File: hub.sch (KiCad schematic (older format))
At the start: 22 parts, among them J1 USB_C_Receptacle_USB2.0, J6 Conn_01x03, U14 GL850G, U15 K24C02D-O, X2 ECS-2520MV-120-xx

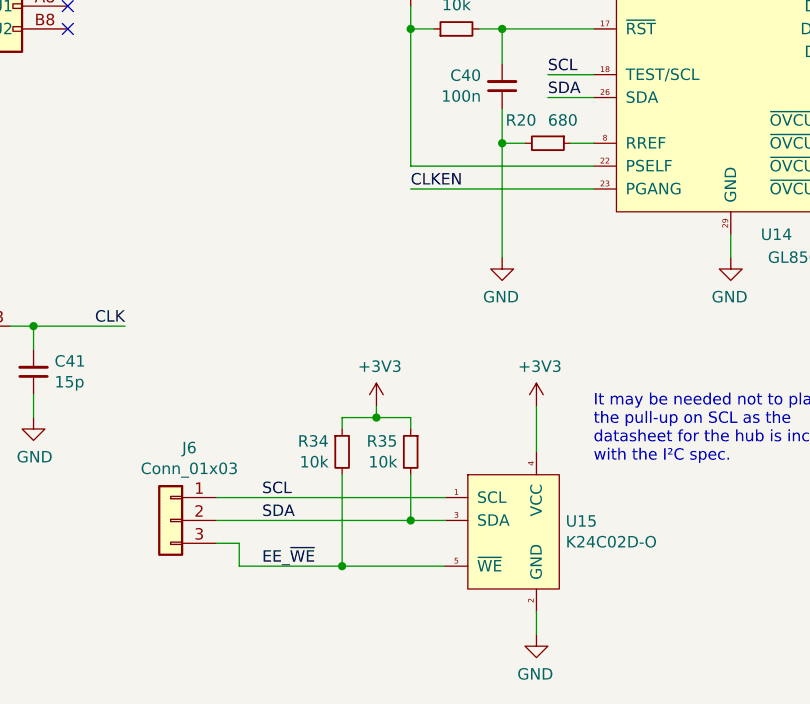
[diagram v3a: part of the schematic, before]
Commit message: sch, pcb: Fix hub startup and use smaller crystals
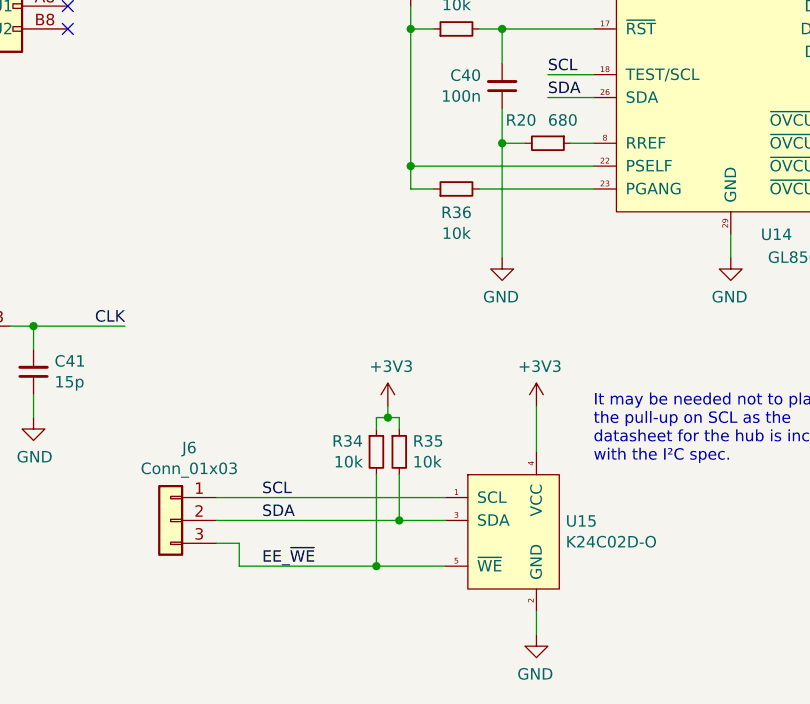
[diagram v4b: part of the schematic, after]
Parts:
- added R36: 10k, Resistor_SMD:R_0603_1608Metric, symbol Device:R_Small
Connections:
- net +3V3: now also R36.1
- net CLKEN: no longer names the net of U14.23 (PGANG)
- net CLKEN: now also R36.2
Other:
- moved on the sheet: R34, R35
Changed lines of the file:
@@
 Wire Wire Line
 	6350 3600 5950 3600
-Wire Wire Line
-	6350 4600 5550 4600
-Text Label 5550 4600 0    50   ~ 0
-CLKEN
 Text Label 5950 3600 0    50   ~ 0
 CLK
@@
 SDA
 $Comp
-L Device:R_Small R?
-U 1 1 5E1E7739
-P 5550 5750
-AR Path="/5DF7E971/5E1E7739" Ref="R?"  Part="1"
-AR Path="/5DFC2583/5E1E7739" Ref="R?"  Part="1"
-AR Path="/5E157F68/5E1E7739" Ref="R35"  Part="1"
-F 0 "R35" H 5608 5796 50  0000 L CNN
-F 1 "10k" H 5608 5705 50  0000 L CNN
-F 2 "Resistor_SMD:R_0603_1608Metric" H 5550 5750 50  0001 C CNN
-F 3 "~" H 5550 5750 50  0001 C CNN
-	1    5550 5750
-	-1   0    0    -1
-$EndComp
-Wire Wire Line
-	5550 5650 5550 5600
+L power:+3V3 #PWR058
+U 1 1 5E1E2F22
+P 5450 5550
+F 0 "#PWR058" H 5450 5400 50  0001 C CNN
+F 1 "+3V3" H 5465 5723 50  0000 C CNN
+F 2 "" H 5450 5550 50  0001 C CNN
+F 3 "" H 5450 5550 50  0001 C CNN
+	1    5450 5550
+	1    0    0    -1
+$EndComp
+Wire Wire Line
+	5500 5650 5500 5600
+Wire Wire Line
+	5450 5550 5450 5600
 $Comp
 L Device:R_Small R?
 U 1 1 5E1FC098
-P 5250 5750
+P 5400 5750
 AR Path="/5DF7E971/5E1FC098" Ref="R?"  Part="1"
 AR Path="/5DFC2583/5E1FC098" Ref="R?"  Part="1"
 AR Path="/5E157F68/5E1FC098" Ref="R34"  Part="1"
-F 0 "R34" H 5191 5796 50  0000 R CNN
-F 1 "10k" H 5191 5705 50  0000 R CNN
-F 2 "Resistor_SMD:R_0603_1608Metric" H 5250 5750 50  0001 C CNN
-F 3 "~" H 5250 5750 50  0001 C CNN
-	1    5250 5750
-	1    0    0    -1
-$EndComp
-Wire Wire Line
-	5250 5650 5250 5600
-Wire Wire Line
-	5700 6250 5250 6250
-Wire Wire Line
-	5250 5850 5250 6250
-Connection ~ 5250 6250
-Wire Wire Line
-	5550 5850 5550 6050
-Connection ~ 5550 6050
-Wire Wire Line
-	5550 6050 5700 6050
+F 0 "R34" H 5341 5796 50  0000 R CNN
+F 1 "10k" H 5341 5705 50  0000 R CNN
+F 2 "Resistor_SMD:R_0603_1608Metric" H 5400 5750 50  0001 C CNN
+F 3 "~" H 5400 5750 50  0001 C CNN
+	1    5400 5750
+	1    0    0    -1
+$EndComp
+Wire Wire Line
+	5400 5650 5400 5600
+Wire Wire Line
+	5700 6250 5400 6250
+Wire Wire Line
+	5400 5850 5400 6250
+Connection ~ 5400 6250
+Wire Wire Line
+	5500 5850 5500 6050
+Connection ~ 5500 6050
+Wire Wire Line
+	5500 6050 5700 6050
+Wire Wire Line
+	5400 5600 5450 5600
 Text Label 4900 6250 0    50   ~ 0
 EE_~WE
@@
 	4800 6150 4700 6150
 Wire Wire Line
-	4800 6250 5250 6250
-Wire Wire Line
-	4700 6050 5550 6050
+	4800 6250 5400 6250
+Wire Wire Line
+	4700 6050 5500 6050
+$Comp
+L Device:R_Small R?
+U 1 1 5E1E7739
+P 5500 5750
+AR Path="/5DF7E971/5E1E7739" Ref="R?"  Part="1"
+AR Path="/5DFC2583/5E1E7739" Ref="R?"  Part="1"
+AR Path="/5E157F68/5E1E7739" Ref="R35"  Part="1"
+F 0 "R35" H 5559 5796 50  0000 L CNN
+F 1 "10k" H 5559 5705 50  0000 L CNN
+F 2 "Resistor_SMD:R_0603_1608Metric" H 5500 5750 50  0001 C CNN
+F 3 "~" H 5500 5750 50  0001 C CNN
+	1    5500 5750
+	1    0    0    -1
+$EndComp
 Wire Wire Line
 	4700 5950 5700 5950
-Connection ~ 5400 5600
-Wire Wire Line
-	5250 5600 5400 5600
-Wire Wire Line
-	5400 5600 5550 5600
-Wire Wire Line
-	5400 5550 5400 5600
-$Comp
-L power:+3V3 #PWR058
-U 1 1 5E1E2F22
-P 5400 5550
-F 0 "#PWR058" H 5400 5400 50  0001 C CNN
-F 1 "+3V3" H 5415 5723 50  0000 C CNN
-F 2 "" H 5400 5550 50  0001 C CNN
-F 3 "" H 5400 5550 50  0001 C CNN
-	1    5400 5550
-	1    0    0    -1
-$EndComp
+Connection ~ 5450 5600
+Wire Wire Line
+	5450 5600 5500 5600
+$Comp
+L Device:R_Small R?
+U 1 1 5EE803EE
+P 5750 4600
+AR Path="/5DF7E971/5EE803EE" Ref="R?"  Part="1"
+AR Path="/5DFC2583/5EE803EE" Ref="R?"  Part="1"
+AR Path="/5E157F68/5EE803EE" Ref="R36"  Part="1"
+F 0 "R36" V 5646 4600 50  0000 C CNN
+F 1 "10k" V 5555 4600 50  0000 C CNN
+F 2 "Resistor_SMD:R_0603_1608Metric" H 5750 4600 50  0001 C CNN
+F 3 "~" H 5750 4600 50  0001 C CNN
+	1    5750 4600
+	0    -1   -1   0
+$EndComp
+Wire Wire Line
+	5550 4500 5550 4600
+Wire Wire Line
+	5550 4600 5650 4600
+Connection ~ 5550 4500
+Wire Wire Line
+	5850 4600 6350 4600
 $EndSCHEMATC
